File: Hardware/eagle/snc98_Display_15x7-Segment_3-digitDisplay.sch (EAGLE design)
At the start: 71 parts, among them M10 IRLML2244, M11 IRLML2244, M4 IRLML2244, M5 IRLML2244, M6 IRLML2244, M7 IRLML2244, M8 IRLML2244, M9 IRLML2244, X1 MICROMATCH-12, X2 MICROMATCH-14, X3 MICROMATCH-12, X4 MICROMATCH-14

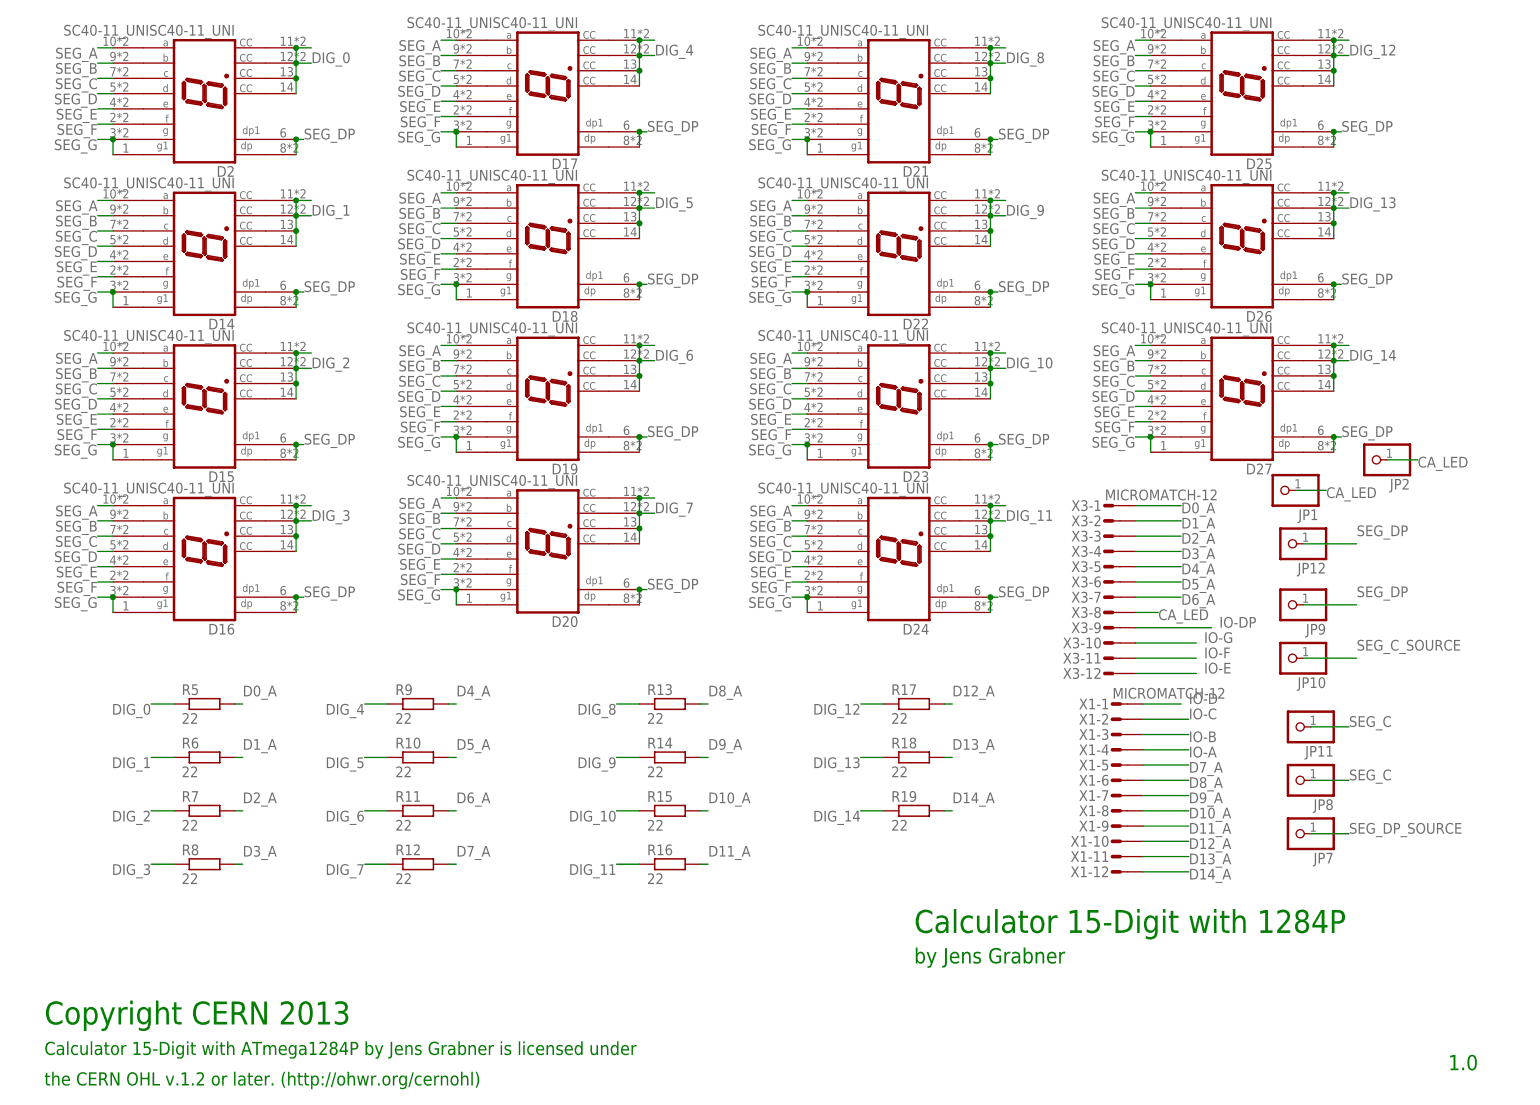
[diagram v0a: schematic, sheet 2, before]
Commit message: Display .. 5x LTD040AUE-101A 3-digit_Display
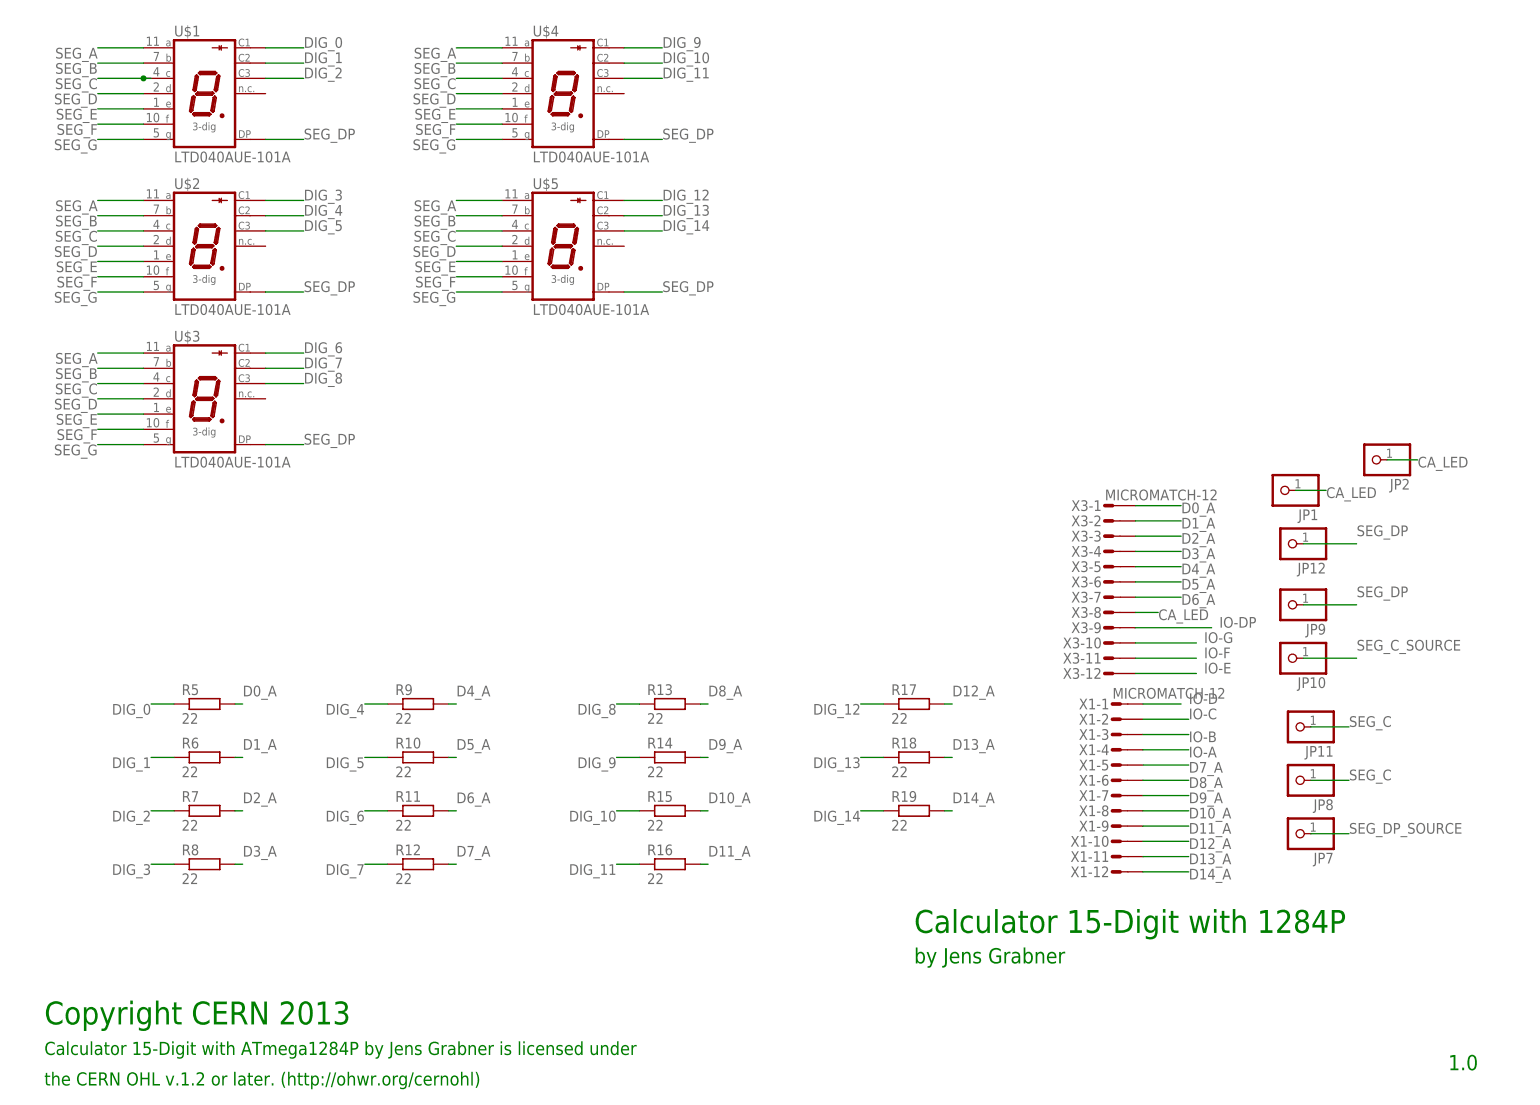
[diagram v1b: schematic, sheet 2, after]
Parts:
- removed D14, D15, D16, D17, D18, D19, D2, D20, D21, D22, D23, D24, D25, D26, D27: SC40-11_UNISC40-11_UNI, display-hp:SC40-11_UNISC40-11_UNI
- added U$1, U$2, U$3, U$4, U$5: LTD040AUE-101A, display_LTD:LTD040AUE-101A
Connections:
- net DIG_0: now also U$1.C1; no longer D2.CC1, D2.CC2, D2.CC3, D2.CC4
- net DIG_1: now also U$1.C2; no longer D14.CC1, D14.CC2, D14.CC3, D14.CC4
- net DIG_10: now also U$4.C2; no longer D23.CC1, D23.CC2, D23.CC3, D23.CC4
- net DIG_11: now also U$4.C3; no longer D24.CC1, D24.CC2, D24.CC3, D24.CC4
- net DIG_12: now also U$5.C1; no longer D25.CC1, D25.CC2, D25.CC3, D25.CC4
- net DIG_13: now also U$5.C2; no longer D26.CC1, D26.CC2, D26.CC3, D26.CC4
- net DIG_14: now also U$5.C3; no longer D27.CC1, D27.CC2, D27.CC3, D27.CC4
- net DIG_2: now also U$1.C3; no longer D15.CC1, D15.CC2, D15.CC3, D15.CC4
- net DIG_3: now also U$2.C1; no longer D16.CC1, D16.CC2, D16.CC3, D16.CC4
- net DIG_4: now also U$2.C2; no longer D17.CC1, D17.CC2, D17.CC3, D17.CC4
- net DIG_5: now also U$2.C3; no longer D18.CC1, D18.CC2, D18.CC3, D18.CC4
- net DIG_6: now also U$3.C1; no longer D19.CC1, D19.CC2, D19.CC3, D19.CC4
- net DIG_7: now also U$3.C2; no longer D20.CC1, D20.CC2, D20.CC3, D20.CC4
- net DIG_8: now also U$3.C3; no longer D21.CC1, D21.CC2, D21.CC3, D21.CC4
- net DIG_9: now also U$4.C1; no longer D22.CC1, D22.CC2, D22.CC3, D22.CC4
- net SEG_A: now also U$1.A, U$2.A, U$3.A, U$4.A, U$5.A; no longer D14.A, D15.A, D16.A, D17.A, D18.A, D19.A, D2.A, D20.A, D21.A, D22.A, D23.A, D24.A, D25.A, D26.A, D27.A
- net SEG_B: now also U$1.B, U$2.B, U$3.B, U$4.B, U$5.B; no longer D14.B, D15.B, D16.B, D17.B, D18.B, D19.B, D2.B, D20.B, D21.B, D22.B, D23.B, D24.B, D25.B, D26.B, D27.B
- net SEG_C: now also U$1.C, U$2.C, U$3.C, U$4.C, U$5.C; no longer D14.C, D15.C, D16.C, D17.C, D18.C, D19.C, D2.C, D20.C, D21.C, D22.C, D23.C, D24.C, D25.C, D26.C, D27.C
- net SEG_D: now also U$1.D, U$2.D, U$3.D, U$4.D, U$5.D; no longer D14.D, D15.D, D16.D, D17.D, D18.D, D19.D, D2.D, D20.D, D21.D, D22.D, D23.D, D24.D, D25.D, D26.D, D27.D
- net SEG_DP: now also U$1.DP, U$2.DP, U$3.DP, U$4.DP, U$5.DP; no longer D14.DP, D14.DP1, D15.DP, D15.DP1, D16.DP, D16.DP1, D17.DP, D17.DP1, D18.DP, D18.DP1, D19.DP, D19.DP1, D2.DP, D2.DP1, D20.DP, D20.DP1, D21.DP, D21.DP1, D22.DP, D22.DP1, D23.DP, D23.DP1, D24.DP, D24.DP1, D25.DP, D25.DP1, D26.DP, D26.DP1, D27.DP, D27.DP1
- net SEG_E: now also U$1.E, U$2.E, U$3.E, U$4.E, U$5.E; no longer D14.E, D15.E, D16.E, D17.E, D18.E, D19.E, D2.E, D20.E, D21.E, D22.E, D23.E, D24.E, D25.E, D26.E, D27.E
- net SEG_F: now also U$1.F, U$2.F, U$3.F, U$4.F, U$5.F; no longer D14.F, D15.F, D16.F, D17.F, D18.F, D19.F, D2.F, D20.F, D21.F, D22.F, D23.F, D24.F, D25.F, D26.F, D27.F
- net SEG_G: now also U$1.G, U$2.G, U$3.G, U$4.G, U$5.G; no longer D14.G, D14.G1, D15.G, D15.G1, D16.G, D16.G1, D17.G, D17.G1, D18.G, D18.G1, D19.G, D19.G1, D2.G, D2.G1, D20.G, D20.G1, D21.G, D21.G1, D22.G, D22.G1, D23.G, D23.G1, D24.G, D24.G1, D25.G, D25.G1, D26.G, D26.G1, D27.G, D27.G1
